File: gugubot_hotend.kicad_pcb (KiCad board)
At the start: 4 copper layers, 63 x 36 mm, 79 parts, among them J1 Power +24V, J2 TEMP_SENSOR, J3 X_ENDSTOP, J4 PROBE, J5 FAN1, J6 FAN2, J7 Heater, J8 Extruder_motor, J9 USB_C_Receptacle_USB2.0, Q1 WST4041, Q2 FH3400C, Q3 WST4041, Q4 FH3400C, Q5 WST4041, Q6 FH3400C, Q7 WST4041, SW1 BOOTSEL, U1 W25Q16JVUXIQ, U2 RY8310, U3 RP2040, U4 TLV70233_SOT23-5, U5 ADXL345BCCZ-RL7, U6 TMC2209, Y1 12MHz

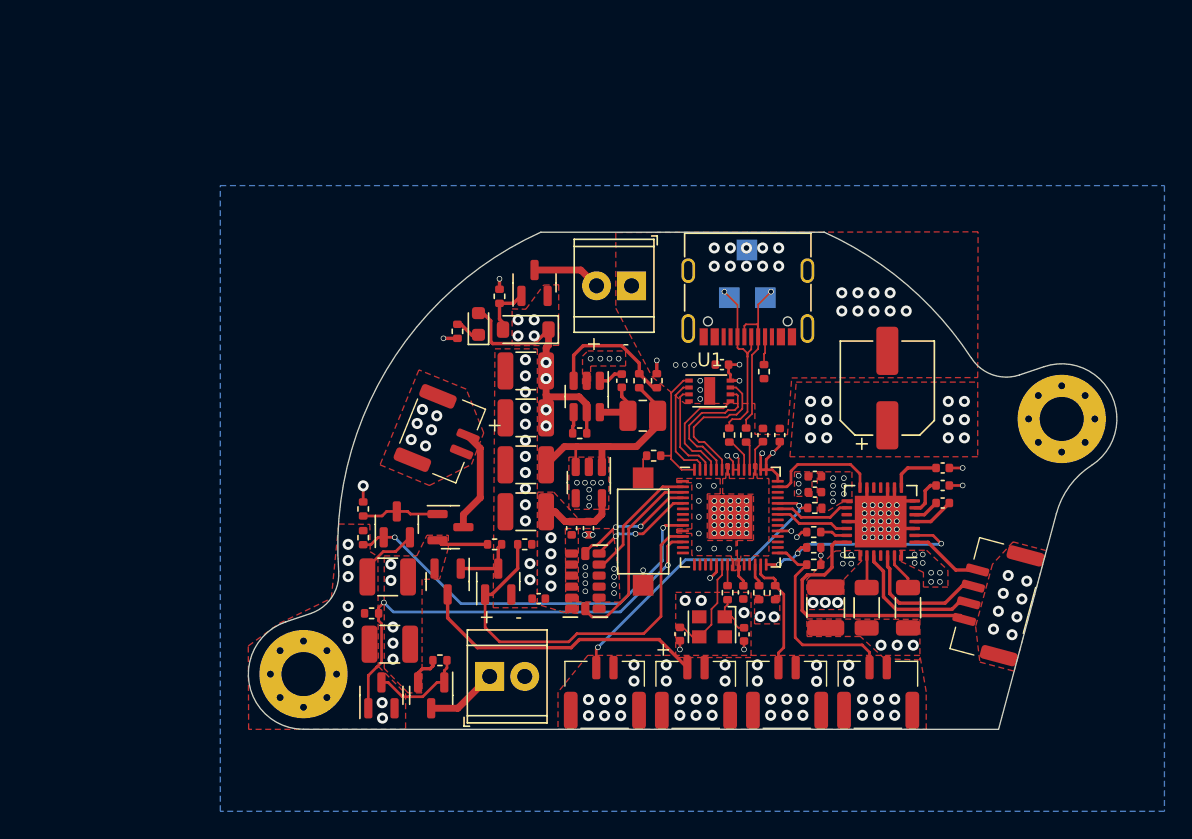
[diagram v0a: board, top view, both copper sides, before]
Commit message: add hall board
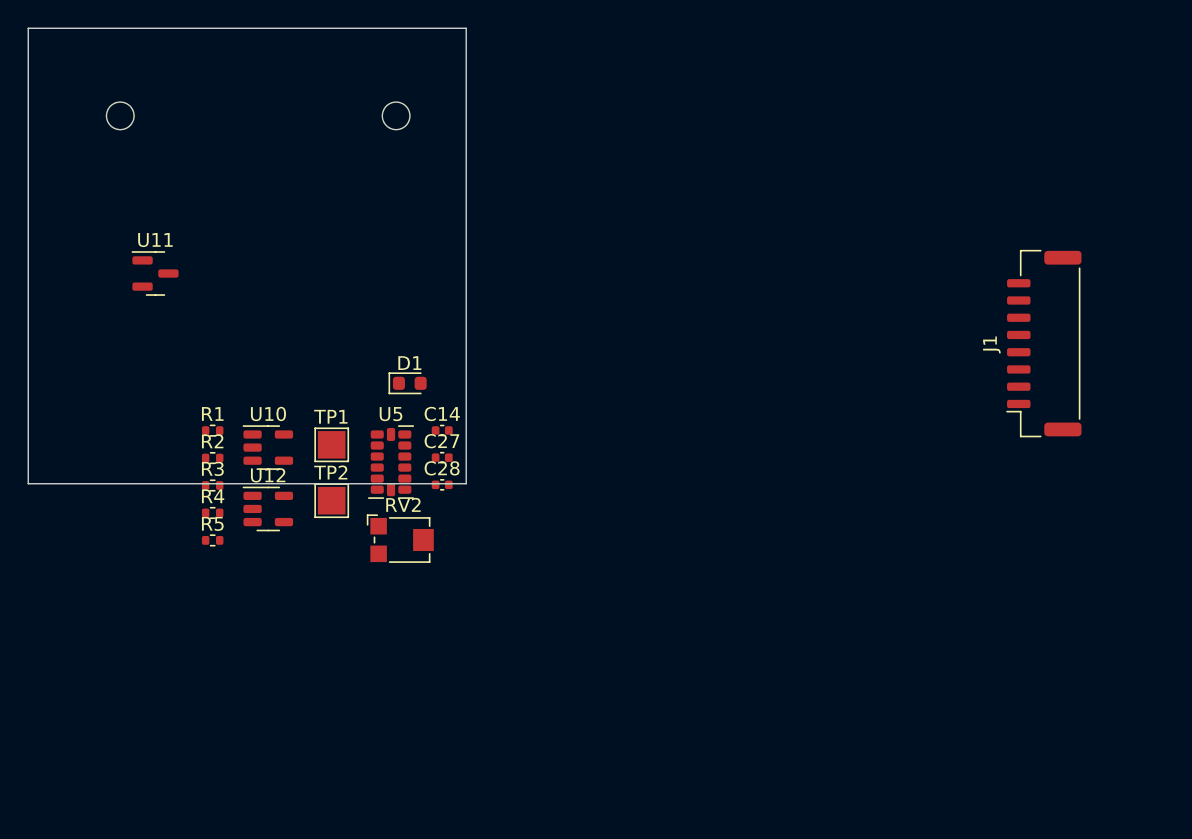
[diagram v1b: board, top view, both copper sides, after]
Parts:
- removed C1: 100uF 25V, Capacitor_SMD:CP_Elec_6.3x5.8
- removed C10, C16, C20, C21, C3, C5, C8: 100nF, Capacitor_SMD:C_0402_1005Metric
- removed C11, C22: 100pF, Capacitor_SMD:C_0402_1005Metric
- removed C12: 1uF, Capacitor_SMD:C_0402_1005Metric
- removed C13, C7: 47uF 16V, Capacitor_SMD:C_1210_3225Metric
- removed C15, C18, C19, C2, C9: 10uF 50V, Capacitor_SMD:C_1210_3225Metric
- removed C23: 22nF, Capacitor_SMD:C_0402_1005Metric
- removed C24: 2.2uF, Capacitor_SMD:C_0402_1005Metric
- removed C4, C6: 18pF, Capacitor_SMD:C_0402_1005Metric
- removed D3: POWER_LED, LED_SMD:LED_0603_1608Metric
- removed H1, H2: MountingHole_Pad, MountingHole:MountingHole_3.2mm_M3_Pad_Via
- removed J2: TEMP_SENSOR, Connector_GH:GH_1.25_1x02_Horizontal
- removed J3: X_ENDSTOP, Connector_GH:GH_1.25_1x02_Horizontal
- removed J4: PROBE, Connector_GH:GH_1.25_1x02_Horizontal
- removed J5: FAN1, Connector_GH:GH_1.25_1x02_Horizontal
- removed J6: FAN2, Connector_GH:GH_1.25_1x02_Horizontal
- removed J7: Heater, TerminalBlock_TE-Connectivity:TerminalBlock_TE_282834-2_1x02_P2.54mm_Horizontal
- removed J8: Extruder_motor, Connector_GH:GH_1.25_1x04_Veritical
- removed J9: USB_C_Receptacle_USB2.0, Connector_USB:USB_C_Receptacle_G-Switch_GT-USB-7010ASV
- removed L1: 4.7uH, Inductor_SMD:L_1008_2520Metric
- removed Q1, Q3, Q5, Q7: WST4041, Package_TO_SOT_SMD:SOT-23
- removed Q2, Q4, Q6: FH3400C, Package_TO_SOT_SMD:SOT-23
- removed R11: 4.7K, Resistor_SMD:R_0402_1005Metric
- removed R12, R13, R16, R17, R19, R23, R7, R9: 10K, Resistor_SMD:R_0402_1005Metric
- removed R14, R18, R20: 1M, Resistor_SMD:R_0402_1005Metric
- removed R15: 20K, Resistor_SMD:R_0402_1005Metric
- removed R21, R22: 180m, Resistor_SMD:R_1206_3216Metric
- removed R24, R25: 1K, Resistor_SMD:R_0402_1005Metric
- removed R6: 27R, Resistor_SMD:R_0402_1005Metric
- removed R8: 52.5K, Resistor_SMD:R_0402_1005Metric
- removed SW1: BOOTSEL, Button_Switch_SMD:SW_SPST_CK_RS282G05A3
- removed TP3: GND, TestPoint:TestPoint_Pad_1.5x1.5mm
- removed U1: W25Q16JVUXIQ, Package_SON:USON-8-1EP_3.0x2.0mm_P0.5mm
- removed U2: RY8310, Package_TO_SOT_SMD:SOT-23-6
- removed U3: RP2040, Package_DFN_QFN:QFN-56-1EP_7x7mm_P0.4mm_EP3.2x3.2mm
- removed U4: TLV70233_SOT23-5, Package_TO_SOT_SMD:SOT-23-5
- removed U6: TMC2209, Package_DFN_QFN:QFN-28-1EP_5x5mm_P0.5mm_EP3.75x3.75mm
- removed Y1: 12MHz, Oscillator:Oscillator_SMD_Kyocera_KC2520Z-4Pin_2.5x2.0mm
- added C27: 100nF, Capacitor_SMD:C_0402_1005Metric, F.Cu at (130.3, 108.6)
- added C28: 100nF, Capacitor_SMD:C_0402_1005Metric, F.Cu at (130.3, 110.6)
- added RV2: R_Potentiometer_Small, Potentiometer_SMD:Potentiometer_Bourns_TC33X_Vertical, F.Cu at (127.5, 114.6)
- added U10: TLV70233_SOT23-5, Package_TO_SOT_SMD:SOT-23-5, F.Cu at (117.7, 107.9)
- added U11: DRV5033AJxDBZ, Package_TO_SOT_SMD:SOT-23, F.Cu at (109.6, 95.2)
- added U12: TL331, Package_TO_SOT_SMD:SOT-23-5, F.Cu at (117.7, 112.3)
- D1: value BZT52C12 -> LED; footprint Diode_SMD:D_SOD-123 -> LED_SMD:LED_0603_1608Metric
- J1: value Power +24V -> Conn_01x08_Socket; footprint TerminalBlock_TE-Connectivity:TerminalBlock_TE_282834-2_1x02_P2.54mm_Horizontal -> Connector_JST:JST_GH_SM08B-GHS-TB_1x08-1MP_P1.25mm_Horizontal
- R1, R3: value 10K -> 0R
- R2: value 5.1K -> 0R
- R4: value 27K -> 0R
- R5: value 27R -> 1K
- TP1: value D- -> PWR; footprint TestPoint:TestPoint_Pad_1.5x1.5mm -> TestPoint:TestPoint_Pad_2.0x2.0mm; moved to F.Cu
- TP2: value D+ -> GND; footprint TestPoint:TestPoint_Pad_1.5x1.5mm -> TestPoint:TestPoint_Pad_2.0x2.0mm; moved to F.Cu
- moved R2 40.5 mm to (113.7, 108.6), turned to 0 degrees
- moved R5 39.4 mm to (113.7, 114.6), turned to 0 degrees
- moved TP2 34.7 mm to (122.3, 111.7), turned to 0 degrees
- moved TP1 30.7 mm to (122.3, 107.7), turned to 0 degrees
- moved J1 30.2 mm to (174.0, 100.3), turned to 90 degrees
- moved R3 26.9 mm to (113.7, 110.6), turned to 0 degrees
- moved R1 23.0 mm to (113.7, 106.6), turned to 0 degrees
- moved R4 22.1 mm to (113.7, 112.6), turned to 0 degrees
- moved U5 16.5 mm to (126.6, 108.9)
- moved C14 11.8 mm to (130.3, 106.6), turned to 0 degrees
- moved D1 9.27 mm to (128.0, 103.2), turned to 0 degrees
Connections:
- D1 pad 1: +24V -> Net-(D1-K)
- J1 pad 1: GND -> +5V
- J1 pad 2: Net-(J1-Pin_2) -> GND
- R1 pad 1: Net-(D1-A) -> Net-(J1-Pin_4)
- R1 pad 2: GND -> Net-(U5-SDO/ADDR)
- R2 pad 1: Net-(J9-CC1) -> Net-(J1-Pin_5)
- R2 pad 2: GND -> Net-(U5-SDA/SDI/SDIO)
- R3 pad 1: +24V -> Net-(J1-Pin_6)
- R3 pad 2: Net-(U2-EN) -> Net-(U5-SCL/SCLK)
- R4 pad 1: Net-(D3-K) -> Net-(J1-Pin_7)
- R4 pad 2: GND -> Net-(U5-~{CS})
- R5 pad 1: Net-(J9-D--PadA7) -> Net-(D1-K)
- R5 pad 2: Net-(U3-USB_DM) -> GND
- TP1 pad 1: Net-(J9-D+-PadA6) -> +5V
- TP2 pad 1: Net-(J9-D--PadA7) -> GND
- U5 pad 12: Net-(U3-GPIO0) -> Net-(U5-SDO/ADDR)
- U5 pad 13: Net-(U3-GPIO3) -> Net-(U5-SDA/SDI/SDIO)
- U5 pad 14: Net-(U3-GPIO2) -> Net-(U5-SCL/SCLK)
- U5 pad 7: Net-(U3-GPIO1) -> Net-(U5-~{CS})
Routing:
- net Net-(Q4-G): track 33.2 -> 0.00 mm, vias 2 -> 0
- net Net-(Q2-G): track 29.1 -> 0.00 mm, vias 2 -> 0
- net Net-(Q6-G): track 28.2 -> 0.00 mm
- net +24V: track 27.2 -> 0.00 mm, vias 42 -> 0
- net Net-(J2-Pin_1): track 22.9 -> 0.00 mm, vias 2 -> 0
- net GND: track 21.7 -> 0.00 mm, vias 185 -> 0
- net Net-(J6-Pin_1): track 21.1 -> 0.00 mm
- net Net-(J8-Pin_1): track 19.5 -> 0.00 mm
- net +3V3: track 18.8 -> 0.00 mm, vias 29 -> 0
- net Net-(U3-GPIO17): track 16.4 -> 0.00 mm, vias 3 -> 0
- net Net-(U4-EN): track 15.3 -> 0.00 mm
- net Net-(J3-Pin_1): track 15.0 -> 0.00 mm
- net Net-(U3-GPIO1): track 13.8 -> 0.00 mm
- net Net-(J9-D--PadA7): track 13.3 -> 0.00 mm, vias 1 -> 0
- net Net-(J9-D+-PadA6): track 13.2 -> 0.00 mm, vias 1 -> 0
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- removed copper zone on F.Cu, net +24V
- removed copper zone on In2.Cu, net +24V
- removed copper zone on F.Cu, net +3V3
- removed copper zone on In2.Cu, net +3V3
- removed copper zone on B.Cu, net GND
- removed copper zone on F.Cu, net GND
- removed copper zone on In1.Cu, net GND
- removed copper zone on F.Cu, net Net-(U3-VREG_VOUT)
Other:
- board size 63 x 36 mm -> 31.8 x 33 mm
- board text removed: "+"
- board text removed: "-"
- board text removed: "3mm"
- board text removed: "7mm DNP"
- board text removed: "Cable Protect Area"
- board text removed: "D+"
- board text removed: "D-"
- board text removed: "GND"
